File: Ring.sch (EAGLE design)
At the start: 4 parts, among them U1 MSP430FR5738IRGET, U2 EM9304V01CS25B

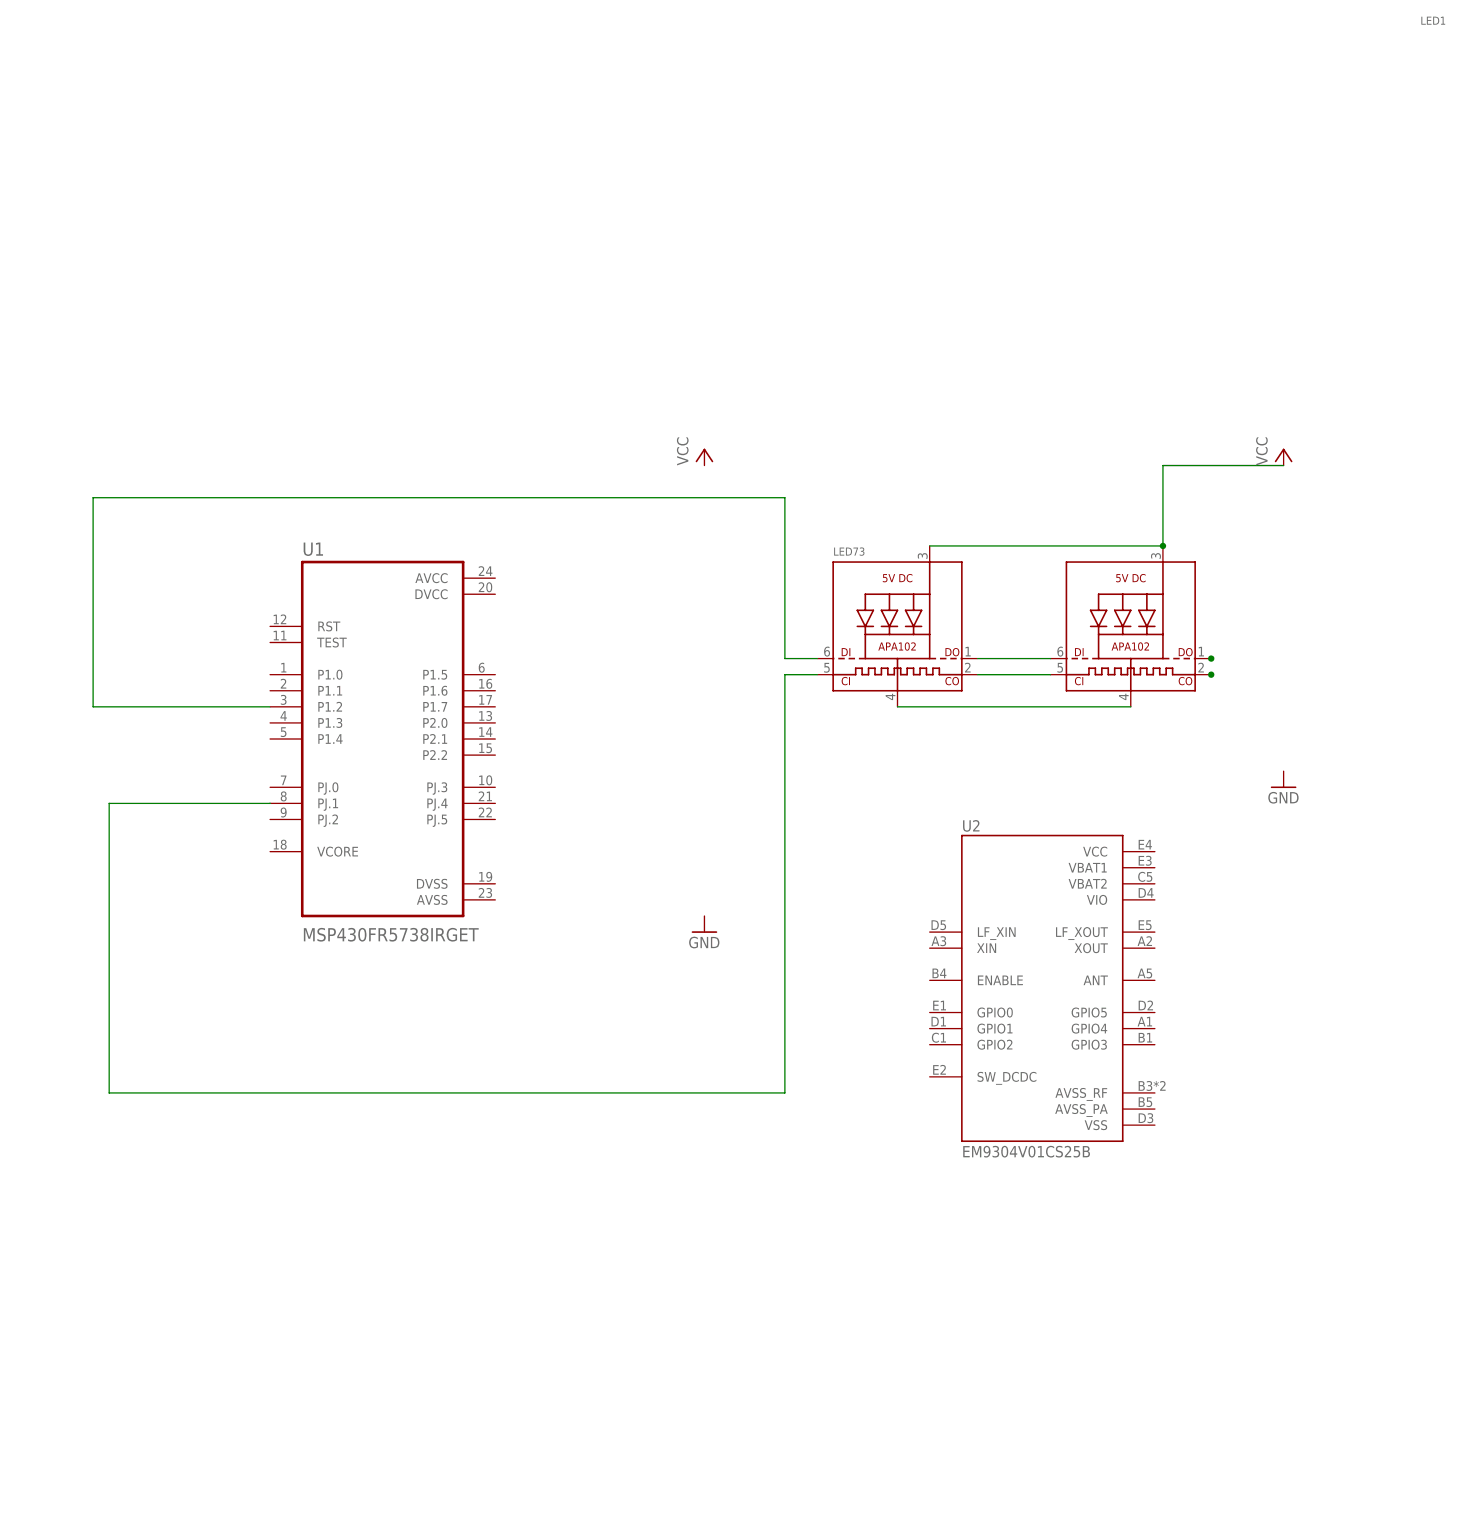
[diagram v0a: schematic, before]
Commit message: Added NRF52382, BQ25, and connections
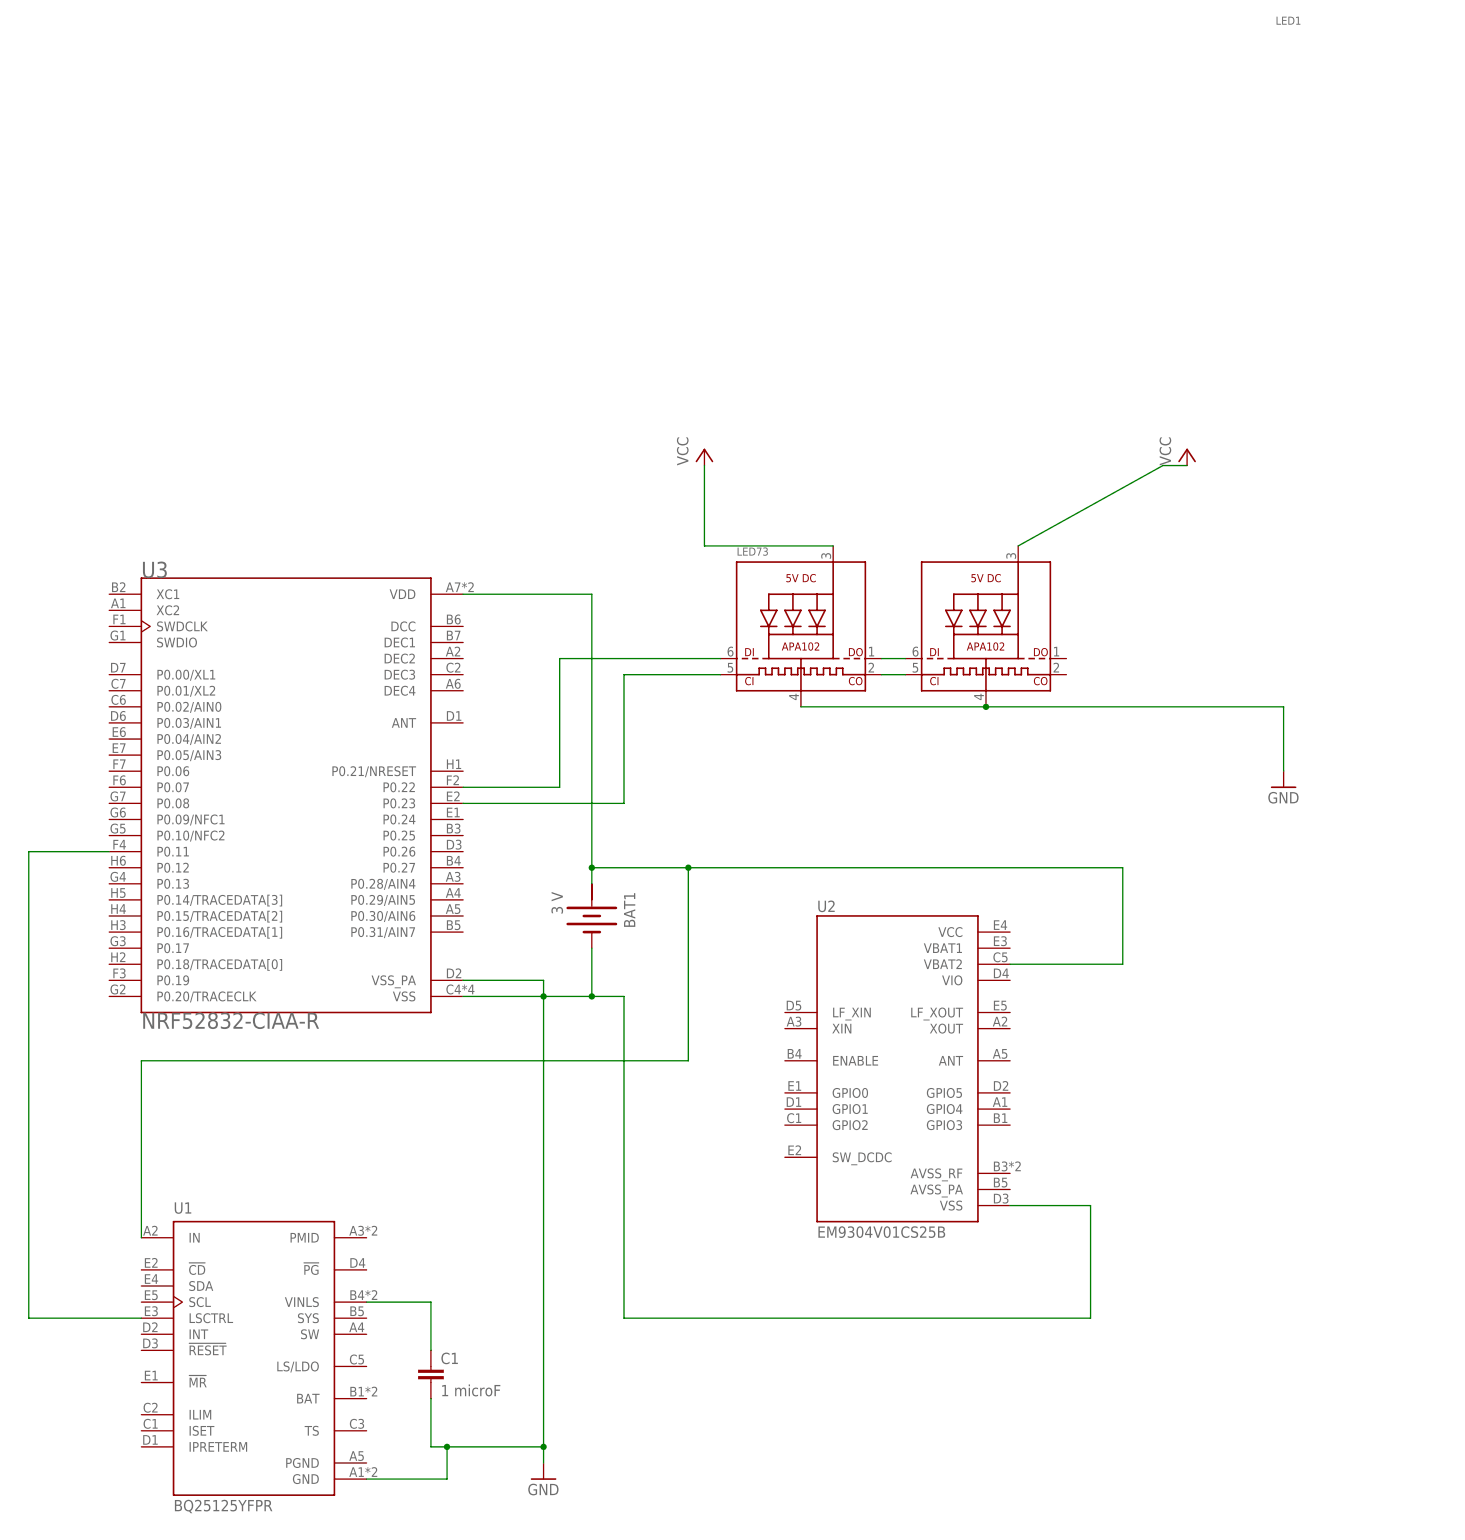
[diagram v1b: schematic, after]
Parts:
- added BAT1: 3 V, special:BATTERY
- added C1: 1 microF, capacitor-wima:C2,5-3
- added U3: NRF52832-CIAA-R, NRF52832-CIAA-R:NRF52832-CIAA-R
- U1: value MSP430FR5738IRGET -> BQ25125YFPR; device MSP430FR5738IRGET:MSP430FR5738IRGET -> BQ25125YFPR:BQ25125YFPR
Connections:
- removed net N$1 (its old number): LED1.DO
- new net N$4: LED73.DI, U3.P0.22
- new net N$8: U1.LSCTRL, U3.P0.11
- net GND: now also BAT1.-, C1.2, U1.GND, U2.VSS, U3.VSS, U3.VSS_PA
- net N$2: now also BAT1.+, U1.IN, U2.VBAT2, U3.VDD; no longer LED1.CKO
- net N$5: now also U3.P0.23; no longer U1.PJ.1
- net N$6: now also C1.1, U1.VINLS; no longer LED73.DI, U1.P1.2
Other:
- moved on the sheet: LED1, LED73, U2

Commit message: Updated connections, deleted bluetooth module
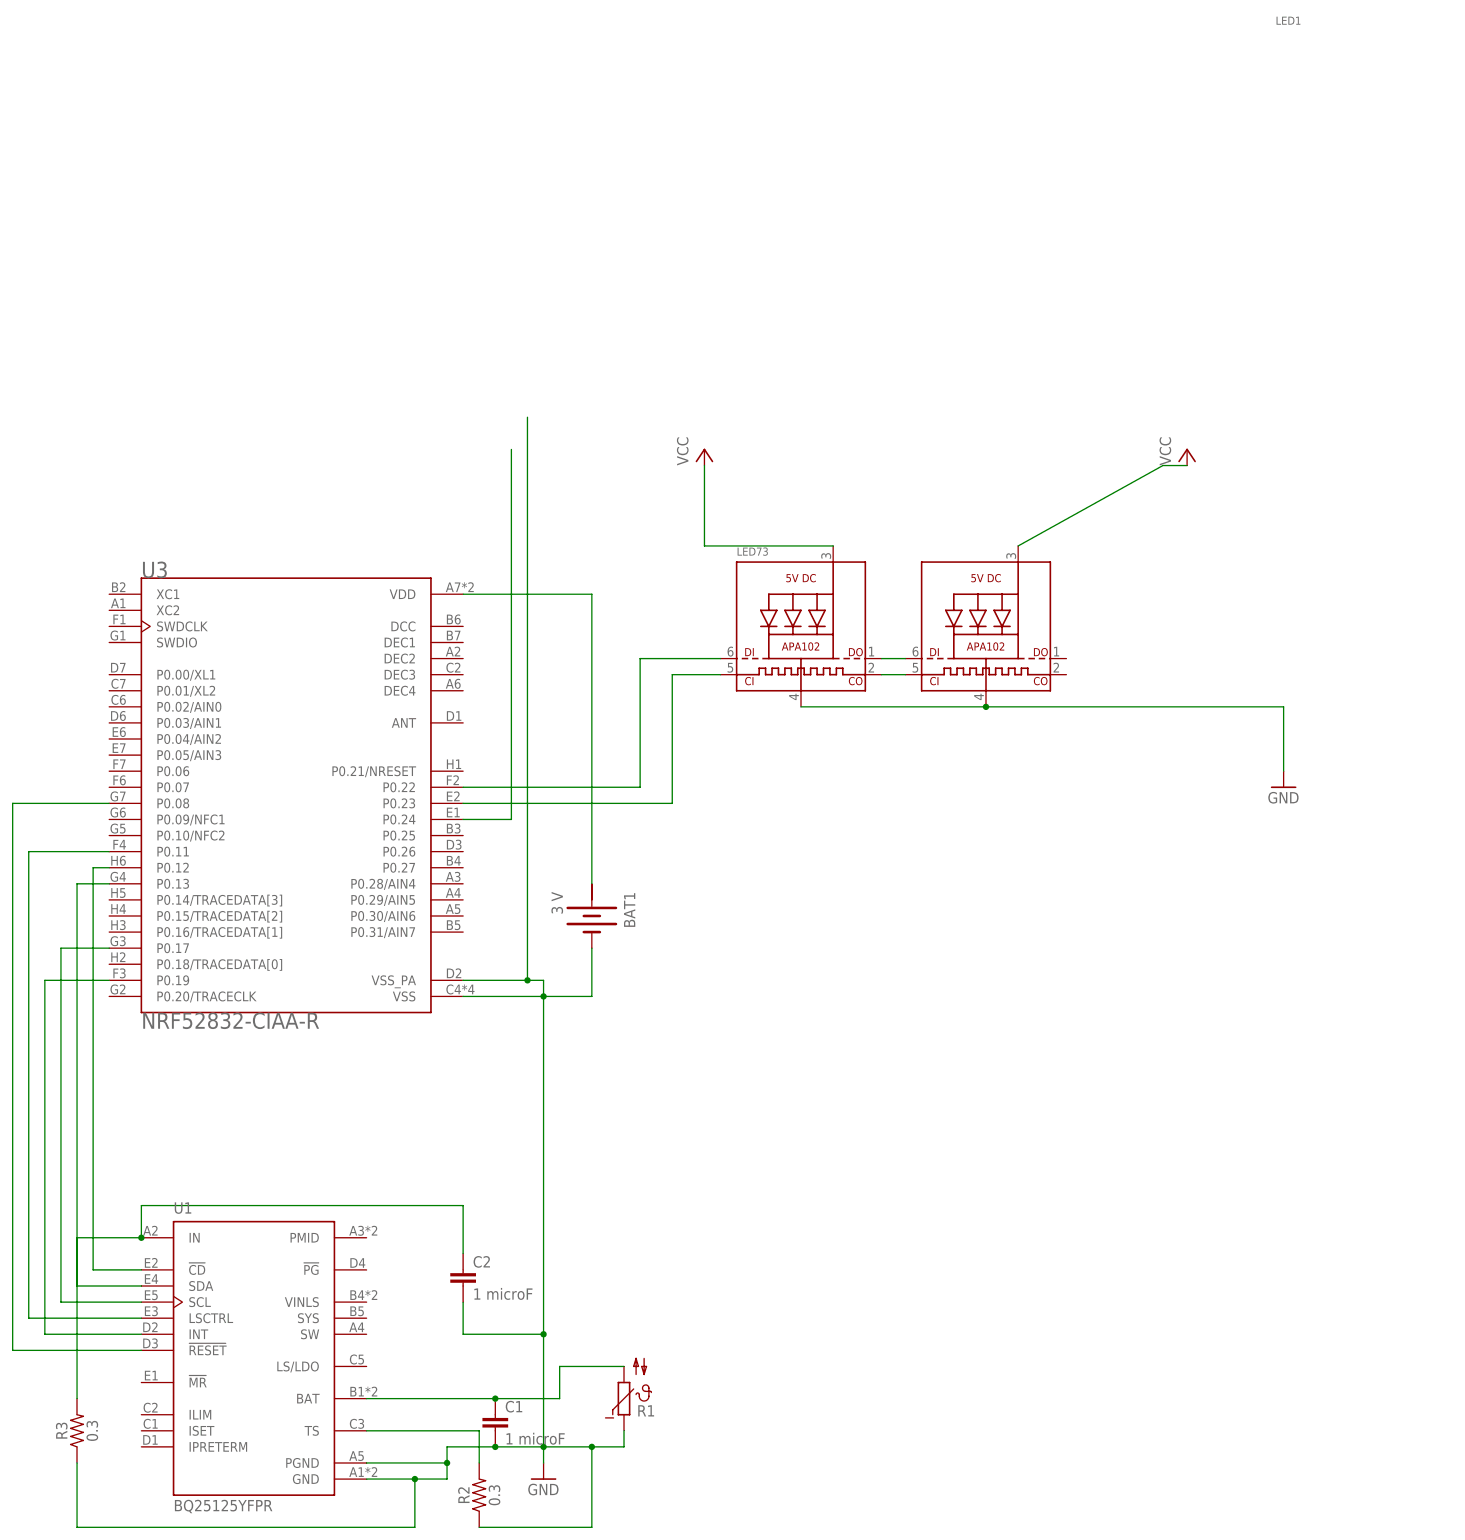
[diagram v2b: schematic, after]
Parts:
- removed U2: EM9304V01CS25B, EM9304V01CS25B:EM9304V01CS25B
- added C2: 1 microF, capacitor-wima:C2,5-3
- added R1: (no value), ptc-ntc:NTC640
- added R2, R3: 0.3, SparkFun-Resistors:0.3OHM-0805-1/8W-1%
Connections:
- new net N$10: U1.SCL, U3.P0.17
- new net N$11: U1.INT, U3.P0.19
- new net N$12: U1.!RESET, U3.P0.08
- new net N$13: C2.1, R3.2, U1.IN
- new net N$14: R2.2, U1.TS
- new net N$15: U3.P0.24
- new net N$7: U1.!CD, U3.P0.12
- new net N$9: U1.SDA, U3.P0.13
- net GND: now also C2.2, R1.1, R2.1, R3.1, U1.PGND; no longer U2.VSS
- net N$2: no longer U1.IN, U2.VBAT2
- net N$6: now also R1.2, U1.BAT; no longer U1.VINLS
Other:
- moved on the sheet: C1
